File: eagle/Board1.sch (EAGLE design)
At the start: 2 parts

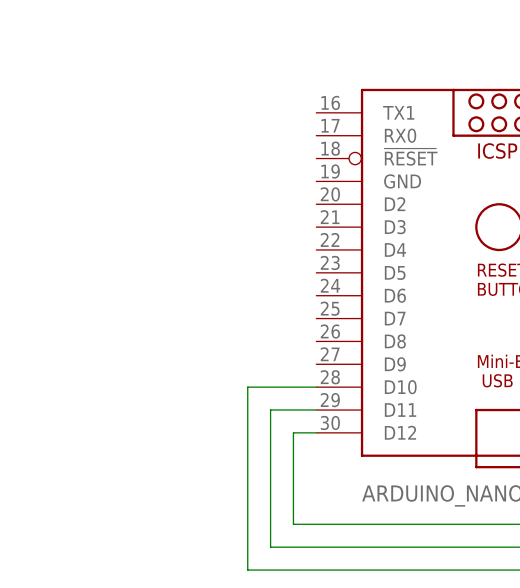
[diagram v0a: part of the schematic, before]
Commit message: Added options for reading binary data file. Latest PCB work.
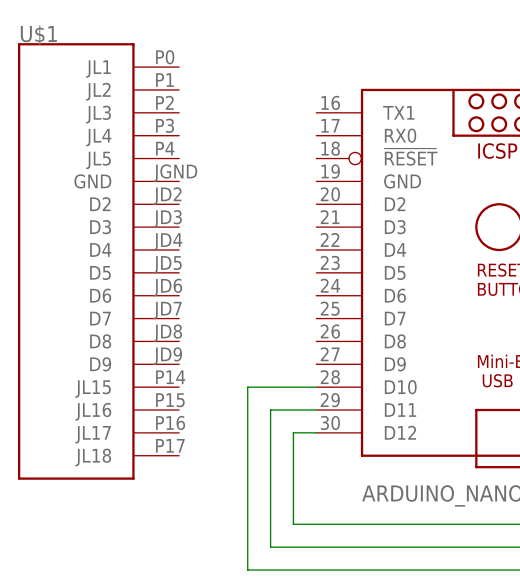
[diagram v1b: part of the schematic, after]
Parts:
- added U$1: JLEFT, cwParts:JLEFT
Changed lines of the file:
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@@
 <part name="USD1" library="cwParts" deviceset="ADA254" device=""/>
 <part name="ARDUINO_NANO1" library="ArduinoNanoV30" deviceset="ARDUINO_NANO" device=""/>
+<part name="U$1" library="cwParts" deviceset="JLEFT" device=""/>
 </parts>
 <sheets>
@@
 <attribute name="VALUE" x="15.24" y="22.86" size="1.778" layer="96"/>
 </instance>
+<instance part="U$1" gate="G$1" x="-15.24" y="53.34" smashed="yes">
+<attribute name="NAME" x="-22.86" y="76.454" size="1.778" layer="95"/>
+</instance>
 </instances>

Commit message: Board 1 nearly complete
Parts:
- removed U$1: JLEFT, cwParts:JLEFT
- added JP1, JP2: (no value), pinhead:PINHD-1X18
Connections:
- new net A0: ARDUINO_NANO1.A0, JP2.14
- new net A1: ARDUINO_NANO1.A1, JP2.13
- new net A2: ARDUINO_NANO1.A2, JP2.12
- new net A3: ARDUINO_NANO1.A3, JP2.11
- new net A4: ARDUINO_NANO1.A4, JP2.10
- new net A5: ARDUINO_NANO1.A5, JP2.9
- new net A6: ARDUINO_NANO1.A6, JP2.8
- new net A7: ARDUINO_NANO1.A7, JP2.7
- new net N$10: ARDUINO_NANO1.D6, JP1.11
- new net N$11: ARDUINO_NANO1.D5, JP1.10
- new net N$12: ARDUINO_NANO1.D4, JP1.9
- new net N$13: ARDUINO_NANO1.D3, JP1.8
- new net N$14: ARDUINO_NANO1.D2, JP1.7
- new net N$15: ARDUINO_NANO1.GND@1, JP1.6
- new net N$7: ARDUINO_NANO1.D9, JP1.14
- new net N$8: ARDUINO_NANO1.D8, JP1.13
- new net N$9: ARDUINO_NANO1.D7, JP1.12
- net N$1: now also JP2.4
- net N$2: now also JP2.6
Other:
- moved on the sheet: ARDUINO_NANO1

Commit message: Latest mods
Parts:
- added BAT1: BAT9V, cwParts:BAT9V
- added JP3, JP4: (no value), pinhead:PINHD-1X3
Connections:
- net N$10 renamed D6
- net N$11 renamed D5
- net N$12 renamed D4
- net N$13 renamed D3
- net N$14 renamed D2
- net N$15 renamed GND1
- net N$2 renamed 5V
- net N$7 renamed D9
- net N$8 renamed D8
- net N$9 renamed D7
- removed net N$1: ARDUINO_NANO1.GND@2, JP2.4, USD1.GND
- new net GND2: ARDUINO_NANO1.GND@2, BAT1.-, JP2.4, USD1.GND
- new net N$16: ARDUINO_NANO1.VIN, BAT1.+
- new net RST: ARDUINO_NANO1.!RESET@1, JP1.5
